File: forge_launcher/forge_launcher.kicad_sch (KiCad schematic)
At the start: 196 parts, among them J1 Conn_02x13_Odd_Even, J10 Screw_Terminal_01x02, J11 Screw_Terminal_01x02, J2 Conn_02x13_Odd_Even, J3 Conn_01x06, J7 Screw_Terminal_01x02, J9 Screw_Terminal_01x02, Q1 STR2P3LLH6(Pfet), Q10 MMBT3904, Q2 2N3904, Q3 MMBT3904, Q4 IPD60R145, Q6 IPD60R145, Q9 MMBT3904, SW10 LAUNCH, SW3 ARM, U1 LT3420, U10 AMC3330, U14 AMC3302, U17 AD7352, U18 IR2127, U2 TLV74318, U23 TLV74325, U3 AD7352, U4 TLV74325, U5 LMO78_03-1.0, U6 4945, U8 AMC3330

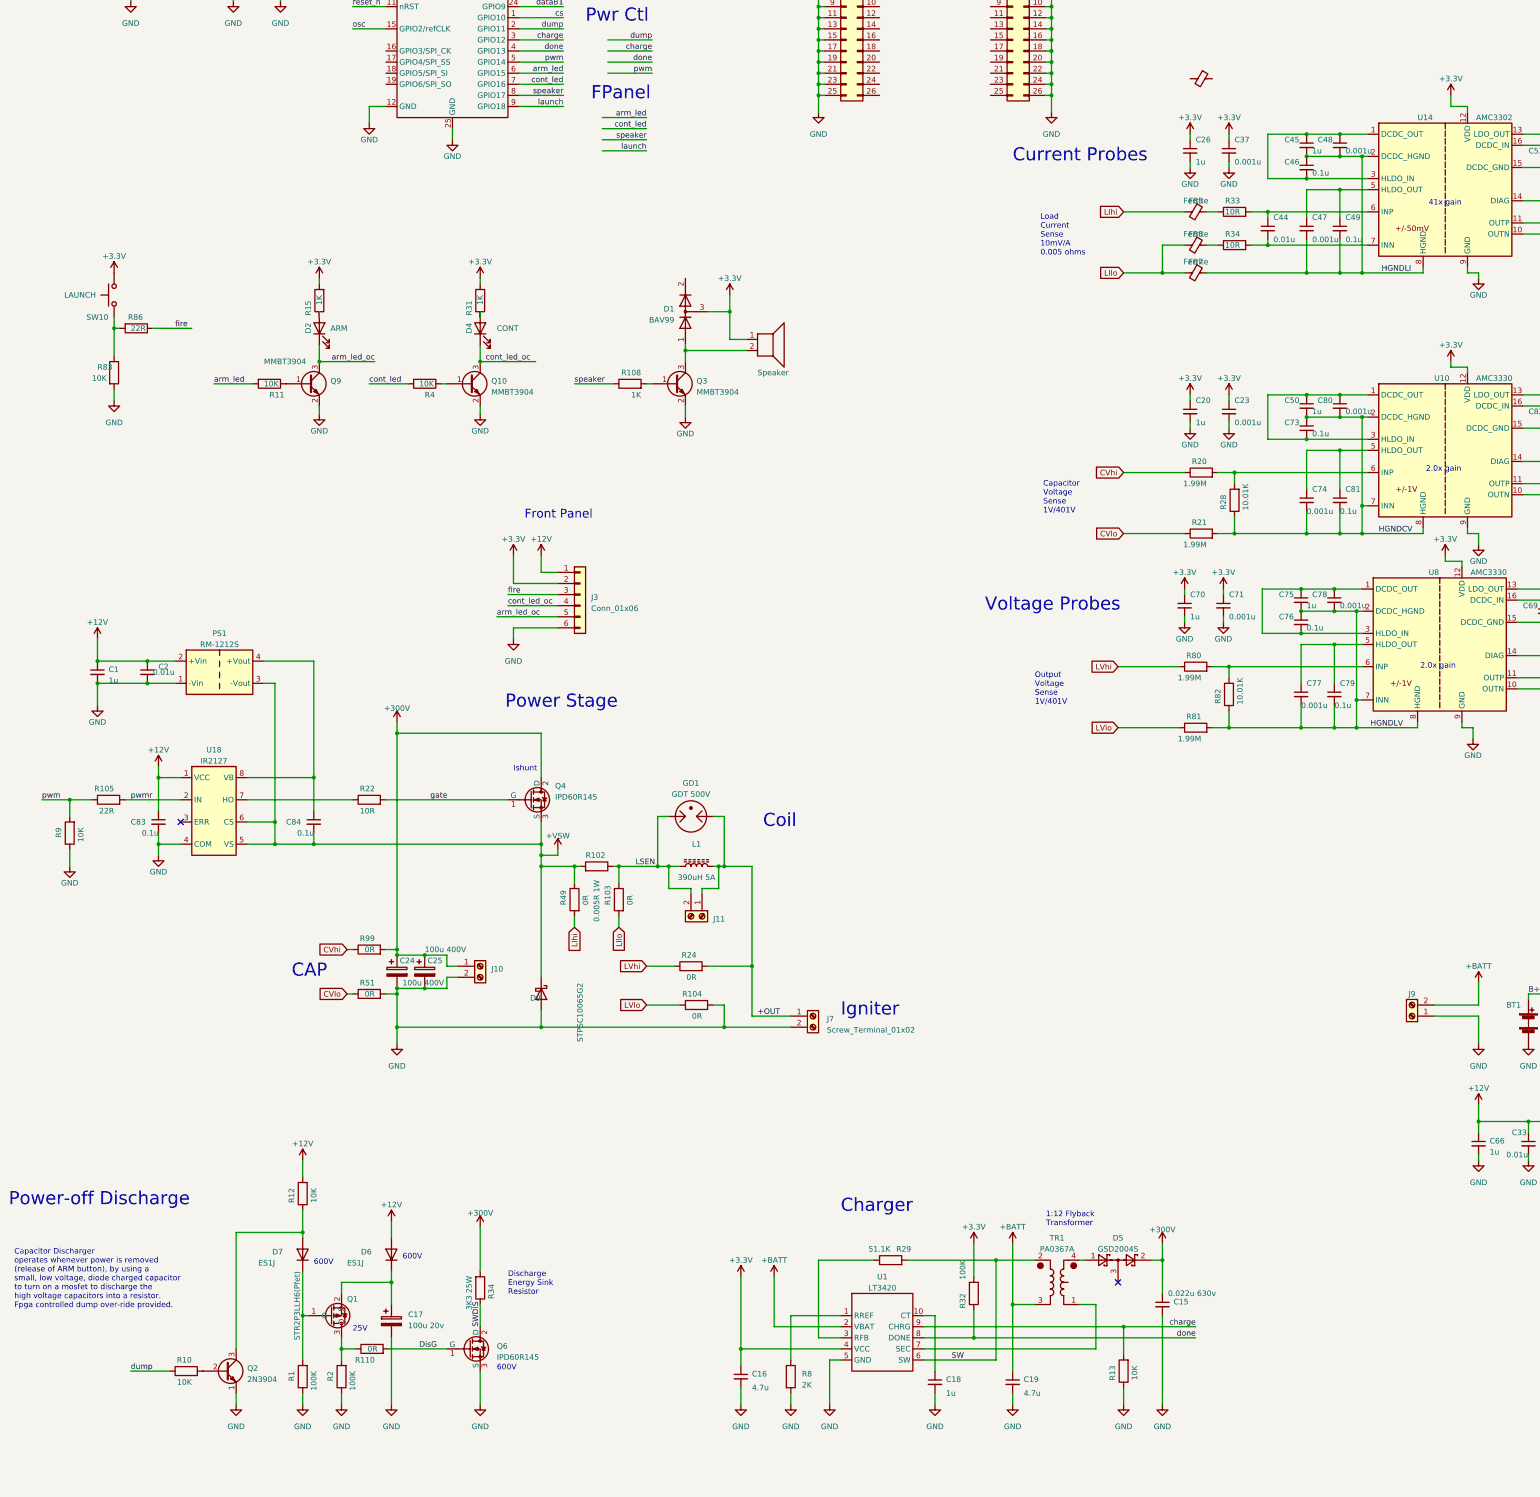
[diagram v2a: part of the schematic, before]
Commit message: Added mosfet so FPGA can eventually replace the LT3420 capacitor charger
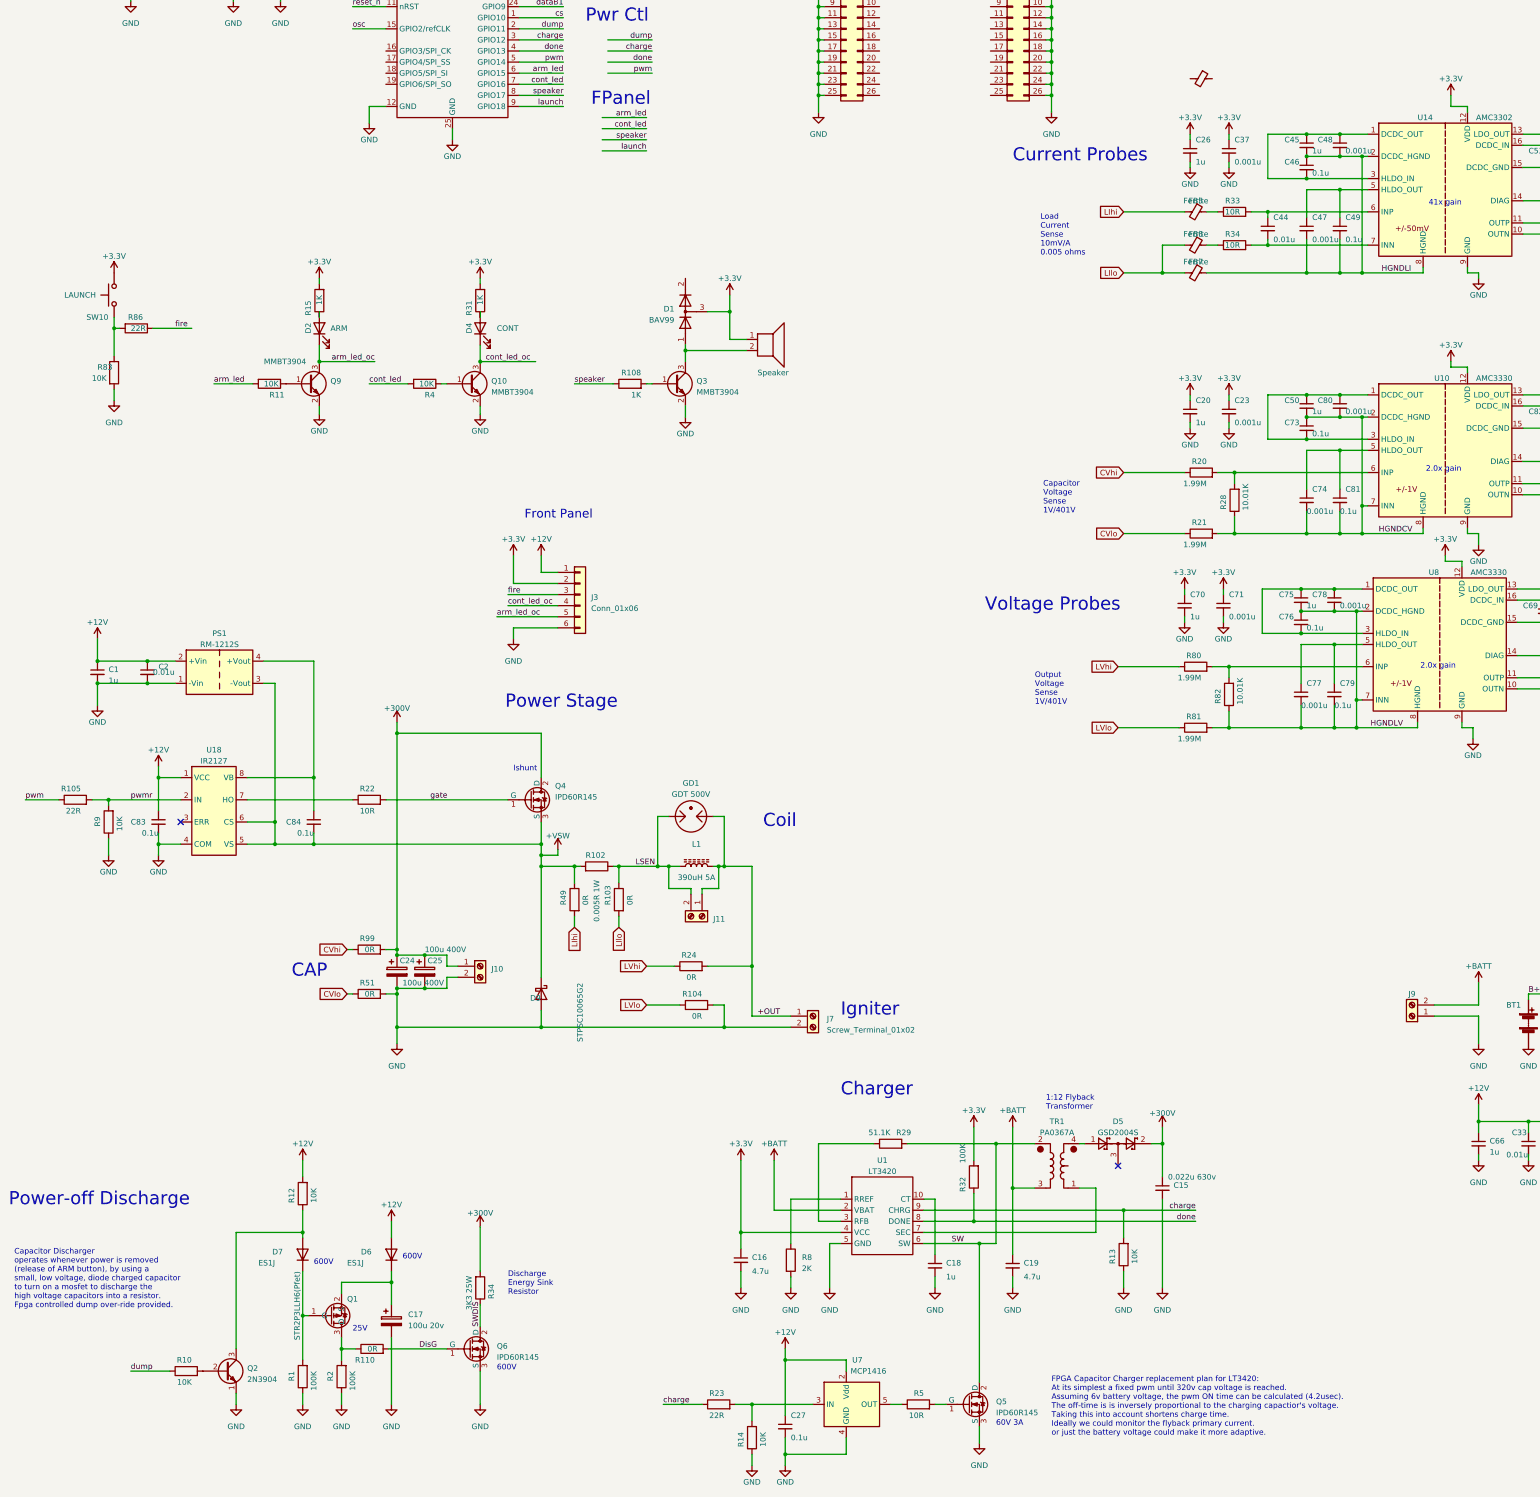
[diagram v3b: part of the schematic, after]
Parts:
- added C27: 0.1u, Capacitor_SMD:C_0603_1608Metric, symbol Device:C_Small
- added Q5: IPD60R145, Package_TO_SOT_SMD:TO-252-2, symbol Simulation_SPICE:NMOS
- added R14: 10K, Resistor_SMD:R_0603_1608Metric, symbol Device:R
- added R23: 22R, Resistor_SMD:R_0603_1608Metric, symbol Device:R
- added R5: 10R, Resistor_SMD:R_0603_1608Metric, symbol Device:R
- added U7: MCP1416, Package_TO_SOT_SMD:SOT-23-5, symbol Driver_FET:MCP1416
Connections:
- net +12V: now also C27.1, U7.2 (Vdd)
- net GND: now also C27.2, Q5.3 (S), R14.1, U7.4 (GND)
- net SW: now also Q5.2 (D)
- net charge: now also R23.1
- net pwm: no longer R9.2
- net pwmr: now also R9.2
- new net: Q5.1 (G), R5.2
- new net: R14.2, R23.2, U7.3 (IN)
- new net: R5.1, U7.5 (OUT)
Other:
- note added: "60V 3A"
- note added: "FPGA Capacitor Charger replacement plan for LT3420: At its simplest a fixed pwm until 320v cap voltage is reached. Assuming 6v battery voltage, the pwm ON time can be calculated (4.2usec). The off-time is is inversely proportional to the charging capactior's voltage. Taking this into account shortens charge time. Ideally we could monitor the flyback primary current. or just the battery voltage co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"
- moved on the sheet: C15, C16, C18, C19, D5, R105, R13, R29, R32, R8, TR1, U1

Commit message: Update to last ver before fork
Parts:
- removed FB2: Ferrite, Inductor_SMD:L_0603_1608Metric, symbol Device:FerriteBead_Small
- removed H10, H11, H12, H13, H14, H15, H5, H6, H7, H8: ~, MountingHole:MountingHole_3mm_Pad, symbol Mechanical:MountingHole_Pad
- removed J10, J11, J7, J9: Screw_Terminal_01x02, TerminalBlock_Phoenix:TerminalBlock_Phoenix_MKDS-1,5-2-5.08_1x02_P5.08mm_Horizontal, symbol Connector:Screw_Terminal_01x02
- removed J3: Conn_01x06, Connector_PinHeader_2.54mm:PinHeader_1x06_P2.54mm_Vertical, symbol Connector_Generic:Conn_01x06
- removed R86: 22R, Resistor_SMD:R_0603_1608Metric, symbol Device:R
- added BT2: ~, Battery:BatteryHolder_Keystone_2462_2xAA, symbol Device:Battery
- added C28, C32, C40: 1u, Capacitor_SMD:C_0603_1608Metric, symbol Device:C_Small
- added C29, C30: 2.2n, Capacitor_SMD:C_0603_1608Metric, symbol Device:C_Small
- added C31: 0.01u, Capacitor_SMD:C_0603_1608Metric, symbol Device:C_Small
- added C35, C36: 4.7u, Capacitor_SMD:C_1206_3216Metric, symbol Device:C_Small
- added FR1, FR2: ~, myspace pcb:button_frog, symbol myspace:frog
- added J4, J7: Jack, myspace pcb:CalTest_CT3151, symbol Connector_Generic:Conn_01x01
- added J5: Conn_01x06, Connector_PinHeader_2.54mm:PinHeader_2x03_P2.54mm_Vertical, symbol Connector_Generic:Conn_02x03_Odd_Even
- added J9: Barrel_Jack, Connector_BarrelJack:BarrelJack_CUI_PJ-063AH_Horizontal, symbol Connector:Barrel_Jack
- added R25: 10.01K, Resistor_SMD:R_0603_1608Metric, symbol Device:R
- added R26, R55: 0, Resistor_SMD:R_0603_1608Metric, symbol Device:R
- added R27: 1.001K, Resistor_SMD:R_0603_1608Metric, symbol Device:R
- added R35, R36: 51R, Resistor_SMD:R_0603_1608Metric, symbol Device:R
- added R37, R38, R41, R42, R45: np, Resistor_SMD:R_0603_1608Metric, symbol Device:R
- added R43, R53: 10K, Resistor_SMD:R_0603_1608Metric, symbol Device:R
- added R44: 3k3, Resistor_SMD:R_0603_1608Metric, symbol Device:R
- added R46: 1K, Resistor_SMD:R_0603_1608Metric, symbol Device:R
- added R47, R48, R50, R54: 22R, Resistor_SMD:R_0603_1608Metric, symbol Device:R
- added SW1: SW_SPST, Button_Switch_THT:SW_E-Switch_EG1224_SPDT_Angled, symbol Switch:SW_SPST
- added U11: AT25xxx, Package_SO:SOIC-8_3.9x4.9mm_P1.27mm, symbol Memory_EEPROM:AT25xxx
- added U12: TLV74318, Package_TO_SOT_SMD:SOT-23-5, symbol myspace:TLV74325_SOT23-5
- added U13: LM809, Package_TO_SOT_SMD:SOT-23, symbol Power_Supervisor:LM809
- added U9: ~, myspace pcb:QFN-24-3x3mm, symbol myspace:SLG47910V
- added X1: ASE-48MHz, Oscillator:Oscillator_SMD_Abracon_ASV-4Pin_7.0x5.1mm_HandSoldering, symbol Oscillator:ASE-xxxMHz
- C16: value 4.7u -> 1u; footprint Capacitor_SMD:C_1206_3216Metric -> Capacitor_SMD:C_0603_1608Metric; DPN 399-C1206C475K5PAC7800CT-ND -> 399-C0603C105K3RAC7867CT-ND
- C18: value 1u -> 4.7u; footprint Capacitor_SMD:C_0603_1608Metric -> Capacitor_SMD:C_1206_3216Metric; DPN 399-C0603C105K3RAC7867CT-ND -> 399-C1206C475K5PAC7800CT-ND
- GD1: footprint (none) -> Capacitor_SMD:C_1812_4532Metric_Pad1.57x3.40mm_HandSolder
- Q5: value IPD60R145 -> IRLML0060TRPBF; footprint Package_TO_SOT_SMD:TO-252-2 -> Package_TO_SOT_SMD:SOT-23
- R13: value 10K -> 51.1K; DPN P10.0KHCT-ND -> P51.1KDBCT-ND; JLC C491211 -> C234563
- R29: value 51.1K -> 100K; DPN P51.1KDBCT-ND -> P100KHCT-ND; JLC C234563 -> C319967
- R32: value 100K -> np; DPN P100KHCT-ND -> P1.00KHCT-ND
- SW3: DPN 360-2595-1-ND -> EG2585-ND
- TR1: footprint myspace pcb:PA0637A Pulse Coil -> myspace pcb:PA0637A Pulse Coil 3D
- U19: footprint Package_DFN_QFN:QFN-24-1EP_3x3mm_P0.4mm_EP1.75x1.6mm_ThermalVias -> myspace pcb:QFN-24-3x3mm
- U5, U6: footprint Package_TO_SOT_THT:TO-220-3_Vertical -> Converter_DCDC:Converter_DCDC_Murata_OKI-78SR_Horizontal
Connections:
- net launch is gone; now on net arm_led: U19.9 (GPIO18)
- net +1V1: now also J1.3 (Pin_3), C32.1, U12.5 (OUT), U9.22 (VDD)
- net +3.3V: now also C18.1, J2.4 (Pin_4), R29.2, R83.1, C28.1, C35.1, C36.1, J5.2 (Pin_2), R37.2, R38.2, R43.1, R44.2, R46.2, R53.1, U11.8 (VCC), U12.1 (IN), U13.3 (VCC), U9.21 (VDDIO), X1.4 (Vdd); no longer R32.2, SW10.2
- net +BATT: now also R25.1
- net +OUT: now also J4.1 (Pin_1)
- net B+: now also J9.1
- net GND: now also C53.2, C69.2, C82.2, H1.1, H2.1, H3.1, H9.1, J1.1 (Pin_1), J2.2 (Pin_2), J2.22 (Pin_22), R32.1, SW10.1, U10.15 (DCDC_GND), U14.15 (DCDC_GND), U8.15 (DCDC_GND), BT2.2 (-), C28.2, C29.2, C30.2, C32.2, C35.2, C36.2, C40.2, J5.5 (Pin_5), J7.1 (Pin_1), J9.2, R26.1, R41.1, R42.1, R45.1, SW1.1 (A), U11.4 (GND), U12.2 (GND), U13.1 (GND), U9.12 (GND), X1.2 (GND); no longer BT1.2 (-), R13.1, R83.2, U19.25 (GND)
- net SW: now also R13.2; no longer R29.2
- net arm_led: now also J1.25 (Pin_25), U9.9 (GPIO18); no longer U19.6 (GPIO15)
- net charge: now also J2.6 (Pin_6), U19.20 (GPIO7), U9.20 (GPIO7); no longer R13.2, U1.9 (CHRG), U19.3 (GPIO12)
- net cont_led: now also J1.5 (Pin_5), U19.23 (GPIO8), U9.23 (GPIO8); no longer U19.7 (GPIO16)
- net cs: now also J1.21 (Pin_21), U19.7 (GPIO16), U9.7 (GPIO16); no longer U19.1 (GPIO10)
- net dataA0: now also J1.13 (Pin_13), U19.3 (GPIO12), U9.3 (GPIO12); no longer U19.13 (GPIO0)
- net dataA1: now also J1.17 (Pin_17), U19.5 (GPIO14), U9.5 (GPIO14); no longer U19.23 (GPIO8)
- net dataB0: now also J1.15 (Pin_15), U19.4 (GPIO13), U9.4 (GPIO13); no longer U19.20 (GPIO7)
- net dataB1: now also J1.19 (Pin_19), U19.6 (GPIO15), U9.6 (GPIO15); no longer U19.24 (GPIO9)
- net done: now also R29.1; no longer R32.1, U19.4 (GPIO13)
- net dump: now also J1.9 (Pin_9), U19.1 (GPIO10), U9.1 (GPIO10); no longer U19.2 (GPIO11)
- net osc: now also J2.16 (Pin_16), R47.1, U9.15 (GPIO2/refCLK)
- net pwm: now also J1.23 (Pin_23), U19.8 (GPIO17), U9.8 (GPIO17); no longer U19.5 (GPIO14)
- net reset_n: now also J2.24 (Pin_24), R48.1, U9.11 (nRST)
- net sclk: now also J1.11 (Pin_11), U19.2 (GPIO11), U9.2 (GPIO11); no longer U19.14 (GPIO1)
- net speaker: now also J2.20 (Pin_20), U19.13 (GPIO0), U9.13 (GPIO0); no longer U19.8 (GPIO17)
- net vina0+: now also C55.1, R63.2; no longer C38.1, R39.2
- net vina0-: now also C57.1, R64.2; no longer C39.1, R40.2
- net vina1+: now also C38.1, R39.2; no longer C54.1, R61.2
- net vina1-: now also C39.1, R40.2; no longer C56.1, R62.2
- net vinb0+: now also C29.1, R35.2
- net vinb0-: now also C30.1, R36.2
- net vinb1+: now also C54.1, R61.2; no longer C55.1, R63.2
- net vinb1-: now also C56.1, R62.2; no longer C57.1, R64.2
- net at TR1.1: now also R32.2, R55.1; no longer U1.7 (SEC)
- net at U1.10 (CT): now also C40.1; no longer C18.1
- net at U1.3 (RFB): now also R13.1; no longer R29.1
- net at R14.2, R23.2, U7.3 (IN): now also U1.9 (CHRG)
- net launch_n: now reaches J1.7 (Pin_7)
- net launch_n: now also U19.24 (GPIO9), R50.1, U9.24 (GPIO9)
- net sleep_n: now reaches U19.10 (nSLEEP)
- net sleep_n: now also J2.26 (Pin_26), U9.10 (nSLEEP)
- net spi_ck: now reaches U19.16 (GPIO3/SPI_CK)
- net spi_ck: now also J2.14 (Pin_14), J5.4 (Pin_4), U11.6 (SCK), U9.16 (GPIO3/SPI_CK)
- net spi_ss: now reaches U19.17 (GPIO4/SPI_SS)
- net spi_ss: now also J2.12 (Pin_12), J5.6 (Pin_6), R44.1, R45.2, U11.1 (~{CS}), U9.17 (GPIO4/SPI_SS)
- net spi_si: now reaches U19.18 (GPIO5/SPI_SI)
- net spi_si: now also J2.10 (Pin_10), J5.1 (Pin_1), U11.5 (MOSI), U9.18 (GPIO5/SPI_SI)
- net spi_so: now reaches U19.19 (GPIO6/SPI_SO)
- net spi_so: now also J2.8 (Pin_8), J5.3 (Pin_3), U11.2 (MISO), U9.19 (GPIO6/SPI_SO)
- net mute_n: now reaches J2.18 (Pin_18)
- net mute_n: now also U19.14 (GPIO1), R54.1, U9.14 (GPIO1)
- new net: R50.2, R83.2, SW10.2
- new net: C31.1, R25.2, R27.2, R35.1
- new net: C31.2, R26.2, R27.1, R36.1
- new net: R55.2, U1.7 (SEC)
- new net: R48.2, U13.2 (~{RESET})
- new net: R53.2, R54.2, SW1.2 (B)
- new net: R46.1, X1.1 (EN)
- new net: R47.2, X1.3 (OUT)
- new net: R37.1, R42.2, U11.7 (~{HOLD})
- new net: R43.2, U12.3 (EN)
- new net: R38.1, R41.2, U11.3 (~{WP})
- new net BINT: BT1.2 (-), BT2.1 (+)
- no-connect marks 13 -> 3
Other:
- note added: "ALT FPGA"
- note added: "Battery Voltage"
- note added: "Capacitor Voltage"
- note added: "IC Charger"
- note added: "LCC Charger"
- note added: "Output Current"
- note added: "Output Voltage"
- note added: "SPI"
- note added: "System"
- note removed: "Charger"
- note removed: "Current Probes"
- note removed: "FPGA Capacitor Charger replacement plan for LT3420: At its simplest a fixed pwm until 320v cap voltage is reached. Assuming 6v battery voltage, the pwm ON time can be calculated (4.2usec). The off-time is is inversely proportional to the charging capactior's voltage. Taking this into account shortens charge time. Ideally we could monitor the flyback primary current. or just the battery voltage co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"
- note removed: "Front Panel"
- note removed: "Voltage Probes"
- moved on the sheet: BT1, C1, C10, C11, C12, C128, C129, C13, C133, C134, C135, C136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
